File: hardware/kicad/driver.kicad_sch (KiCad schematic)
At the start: 38 parts, among them J2 MOTOR A+ A- B+ B-, Q10 CSD88537ND, Q11 CSD88537ND, Q12 CSD88537ND, Q13 CSD88537ND, U2 TMC5160A-TA

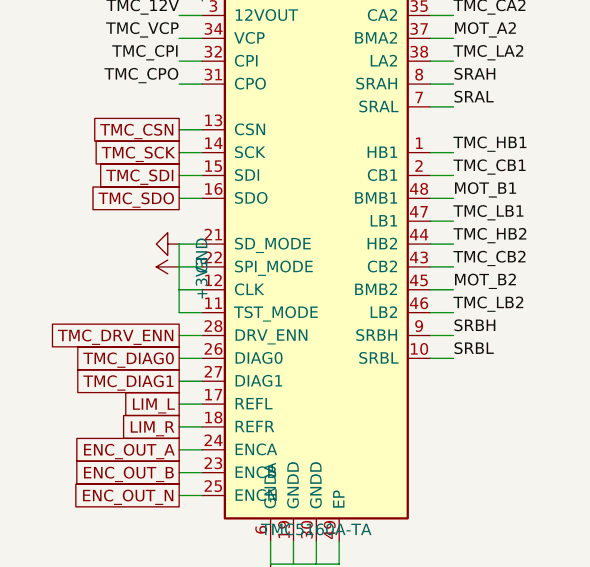
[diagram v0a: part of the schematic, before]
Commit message: Add routed controller PCB, clutch CAD and mill notes
- Schematic: panel ribbon (2x7 IDC) + feed-unit header (JST-XH 7) so all
  connectors fit one 100 mm board edge; fix stub-bridging in the generator.
- PCB (hardware/tools/build_pcb.py): 100x100 mm 4-layer board built from the
  netlist - fixed placement for power/connectors, auto-placed passives,
  GND / split +36V/+3V3 inner planes, Freerouting, post-route power pours,
  GND stitching; fix_planes.py drops plane vias for leftovers;
  check_pcb.py runs DRC with schematic parity. 3D renders in hardware/renders.
  Status: 5 unconnected items + 2 starved thermals left for interactive
  routing (see hardware/kicad/drc.json after check_pcb.py).
- mechanical/clutch: parametric build123d model of the DIY tooth clutch
  (field housing, coil, rotor, armature, leaf springs, output hub/shaft,
  cover), STEP/STL export and VTK renders.
- docs/mill.md: SIEG X3.5D research and the measurements still needed.

Co-Authored-By: Claude Opus 5.5 <noreply@anthropic.com>
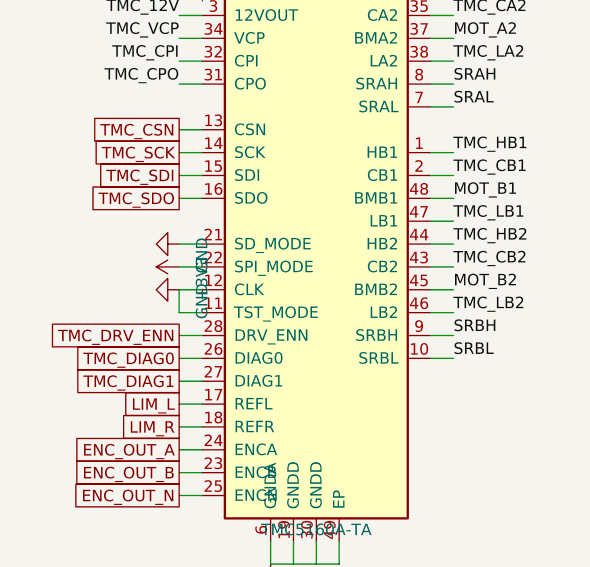
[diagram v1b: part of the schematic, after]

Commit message: Complete LCSC part numbers in the BOM
Every BOM line now has an LCSC number except the Pico module (A1), which
is marked "user-supplied, hand-solder". Parts were checked against the
JLCPCB parts library for spec, Basic/Extended status and stock.

- build_schematic.py: RES_PARTS / CAP_PARTS value+footprint lookup tables
  used by R() / C(), which now raise if a passive has no entry; props for
  the diodes, LEDs, logic ICs, PTC (Littelfuse 2920L050DR, 60 V), IDC
  header (ZHOURI DC3-2.54-14PAS), JST-XH 7p and the Omron B3S-1000 reset
  button.
- Regenerated the schematic sheets, kicad/bom.csv, fab BOM and the README
  missing-LCSC table. PCB, CPL, gerbers and drills are unchanged.

Co-Authored-By: Claude Sonnet 5.5 <noreply@anthropic.com>
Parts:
- C11, C12, C14: LCSC (none) -> C28233; MPN (none) -> Samsung CL21B104KCFNNNE
- C13: LCSC (none) -> C107137; MPN (none) -> Yageo CC0805KRX7R0BB223
- C15: LCSC (none) -> C1779; MPN (none) -> Samsung CL21A475KAQNNNE
- C16: LCSC (none) -> C1623; MPN (none) -> Samsung CL10B474KA8NNNC
- C17: LCSC (none) -> C13585; MPN (none) -> Samsung CL31A106KBHNNNE
- C18: LCSC (none) -> C14663; MPN (none) -> Yageo CC0603KRX7R9BB104
- C19, C21, C23, C25: LCSC (none) -> C64705; MPN (none) -> Samsung CL10B224KB8NNNC
- C20, C22, C24, C26: LCSC (none) -> C86054; MPN (none) -> Murata GRM32ER72A225KA35L
- R10, R11, R12, R13, R14, R15, R16, R17: LCSC (none) -> C25121; MPN (none) -> UNI-ROYAL 0402WGF470KTCE
- R19, R20, R22, R23: LCSC (none) -> C23182; MPN (none) -> UNI-ROYAL 0603WAF470JT5E
- R9: LCSC (none) -> C22939; MPN (none) -> UNI-ROYAL 0603WAF220KT5E
